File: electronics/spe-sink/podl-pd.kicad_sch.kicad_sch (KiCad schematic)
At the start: 18 parts, among them Q1 2N7002P, U1 ATL431LIB, U2 MCP65R41T, U3 AP7375-33

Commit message: PD function board schematic progress
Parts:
- added TEST3: CLIP_HOOK_GREY, Applidyne_Test:KEYSTONE_5118, symbol appli_test_points:CLIP_HOOK_GREY
- C1, C2, C3: footprint CAPC1608* -> Applidyne_Capacitor:CAPC1608X90N
- C4: footprint CAPC2012* -> Applidyne_Capacitor:CAPC2012X110N
- Q1: footprint SOT23 -> Applidyne_SOT:SOT95P240X110-3L16N
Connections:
- net PoDL+: now reaches C3.1, R4.1, R7.1, U3.1 (VIN)
- net PoDL+: now also TEST3.1 (PAD)
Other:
- note added: "Optional SCCP classification circuit would go here!"
- note removed: "Optional SCCP circuit would go here!"
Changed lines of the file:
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@@
   (junction (at 182.88 73.66) (diameter 0) (color 0 0 0 0)
   )
-  (wire (pts (xy 193.04 50.8) (xy 252.73 50.8))
+  (wire (pts (xy 193.04 50.8) (xy 222.25 50.8))
     (stroke (width 0) (type default))
   )
@@
     (effects (font (size 1.27 1.27)) (justify left bottom))
   )
-  (text "Optional SCCP circuit\nwould go here!" (at 223.52 64.77 0)
+  (text "Optional SCCP classification \ncircuit would go here!"
+    (at 228.6 58.42 0)
     (effects (font (size 1.27 1.27)) (justify left bottom))
   )
@@
     (at 198.12 130.81 0)
     (effects (font (size 1.27 1.27)) (justify left bottom))
+  )
+  (hierarchical_label "PoDL+" (shape input) (at 48.26 50.8 180) (fields_autoplaced)
+    (effects (font (size 1.27 1.27)) (justify right))
   )
   (symbol (lib_id "appli_capacitor:56n_X7R_1608M") (at 63.5 63.5 0) (unit 1)
@@
       (effects (font (size 0.889 0.889)) (justify right))
     )
-    (property "Footprint" "CAPC1608*" (at 66.548 65.532 90)
+    (property "Footprint" "Applidyne_Capacitor:CAPC1608X90N" (at 66.548 65.532 90)
       (effects (font (size 0.508 0.508)) hide)
     )
@@
     )
   )
+  (symbol (lib_id "appli_test_points:CLIP_HOOK_GREY") (at 222.25 50.8 270) (unit 1)
+    (in_bom yes) (on_board yes) (dnp no) (fields_autoplaced)
+    (property "Reference" "TEST3" (at 227.33 48.8949 90)
+      (effects (font (size 0.9906 0.9906)) (justify left))
+    )
+    (property "Value" "CLIP_HOOK_GREY" (at 222.25 52.07 0)
+      (effects (font (size 0.9906 0.9906)) (justify left top) hide)
+    )
+    (property "Footprint" "Applidyne_Test:KEYSTONE_5118" (at 220.98 52.07 0)
+      (effects (font (size 0.9906 0.9906)) (justify left top) hide)
+    )
+    (property "Datasheet" "http://www.farnell.com/datasheets/1703983.pdf" (at 217.17 52.07 0)
+      (effects (font (size 0.9906 0.9906)) (justify left bottom) hide)
+    )
+    (property "manf" "KEYSTONE" (at 219.71 52.07 0)
+      (effects (font (size 0.9906 0.9906)) (justify left top) hide)
+    )
+    (property "manf#" "5118" (at 215.9 52.07 0)
+      (effects (font (size 0.9906 0.9906)) (justify left bottom) hide)
+    )
+    (property "Supplier" "Element14" (at 214.63 52.07 0)
+      (effects (font (size 0.9906 0.9906)) (justify left bottom) hide)
+    )
+    (property "Supplier Part No" "2501304" (at 213.36 52.07 0)
+      (effects (font (size 0.9906 0.9906)) (justify left bottom) hide)
+    )
+    (property "Supplier URL" "http://au.element14.com/keystone/5118/test-point-pcb-grey-through-hole/dp/2501304" (at 212.09 52.07 0)
+      (effects (font (size 0.9906 0.9906)) (justify left bottom) hide)
+    )
+    (property "Supplier Price" "0.3" (at 210.82 52.07 0)
+      (effects (font (size 0.9906 0.9906)) (justify left bottom) hide)
+    )
+    (property "Suppier Price Break" "1" (at 209.55 52.07 0)
+      (effects (font (size 0.9906 0.9906)) (justify left bottom) hide)
+    )
+    (pin "1")
+    (instances
+      (project "spe-sink"
+        (path "/f0a501c7-1ad1-4c59-9255-3d6aa4545d8b/d425fecd-d9e0-4566-867f-2251b234bee9"
+          (reference "TEST3") (unit 1)
+        )
+      )
+    )
+  )
   (symbol (lib_id "appli_resistor:20K0_1608M") (at 182.88 74.93 0) (mirror y) (unit 1)
     (in_bom yes) (on_board yes) (dnp no) (fields_autoplaced)
@@
       (effects (font (size 0.889 0.889)) (justify left))
     )
-    (property "Footprint" "CAPC1608*" (at 150.241 81.28 90)
+    (property "Footprint" "Applidyne_Capacitor:CAPC1608X90N" (at 150.241 81.28 90)
       (effects (font (size 0.508 0.508)) hide)
     )
@@
       (effects (font (size 1.27 1.27)) (justify left))
     )
-    (property "Footprint" "SOT23" (at 195.58 99.06 0)
+    (property "Footprint" "Applidyne_SOT:SOT95P240X110-3L16N" (at 195.58 99.06 0)
       (effects (font (size 1.27 1.27) italic) (justify left) hide)
     )
@@
       (effects (font (size 0.889 0.889)) (justify left))
     )
-    (property "Footprint" "CAPC1608*" (at 114.681 106.68 90)
+    (property "Footprint" "Applidyne_Capacitor:CAPC1608X90N" (at 114.681 106.68 90)
       (effects (font (size 0.508 0.508)) hide)
     )
@@
       (effects (font (size 0.889 0.889)) (justify left))
     )
-    (property "Footprint" "CAPC2012*" (at 94.361 66.04 90)
-      (effects (font (size 0.508 0.508)) hide)
-    )
+    (property "Footprint" "Applidyne_Capacitor:CAPC2012X110N" (at 94.361 66.04 90)
+      (effects (font (size 0.508 0.508)) hide)
+    )

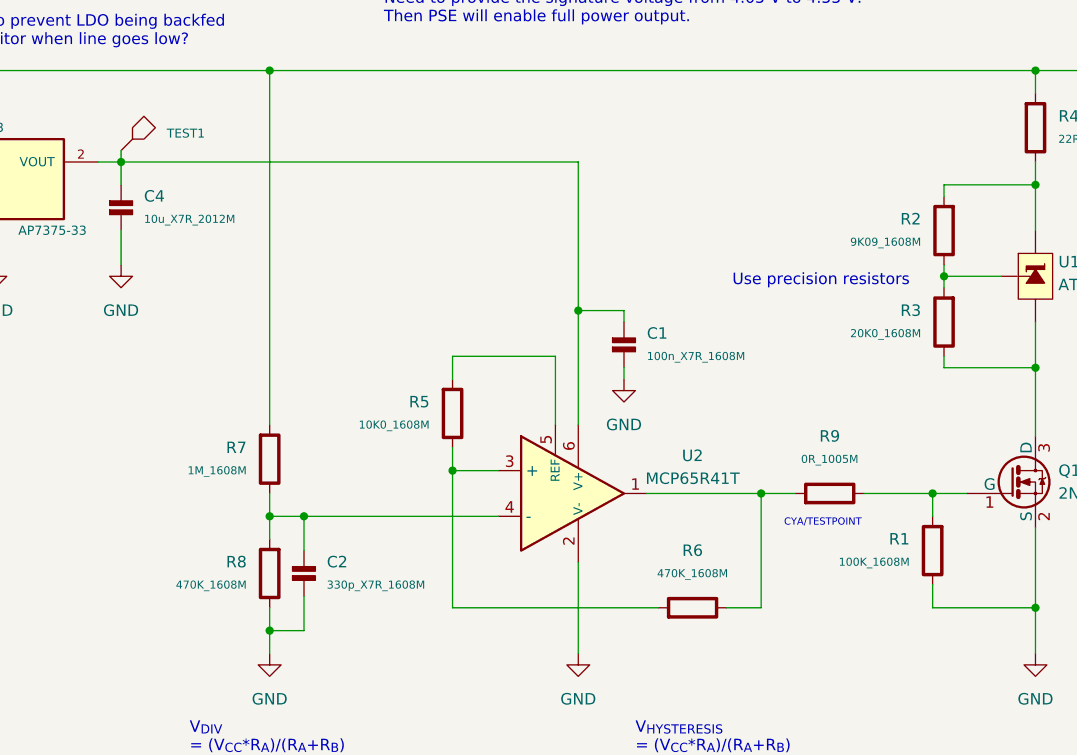
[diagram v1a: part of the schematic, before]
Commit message: PD function board bulk regulator, cleanup, part placement
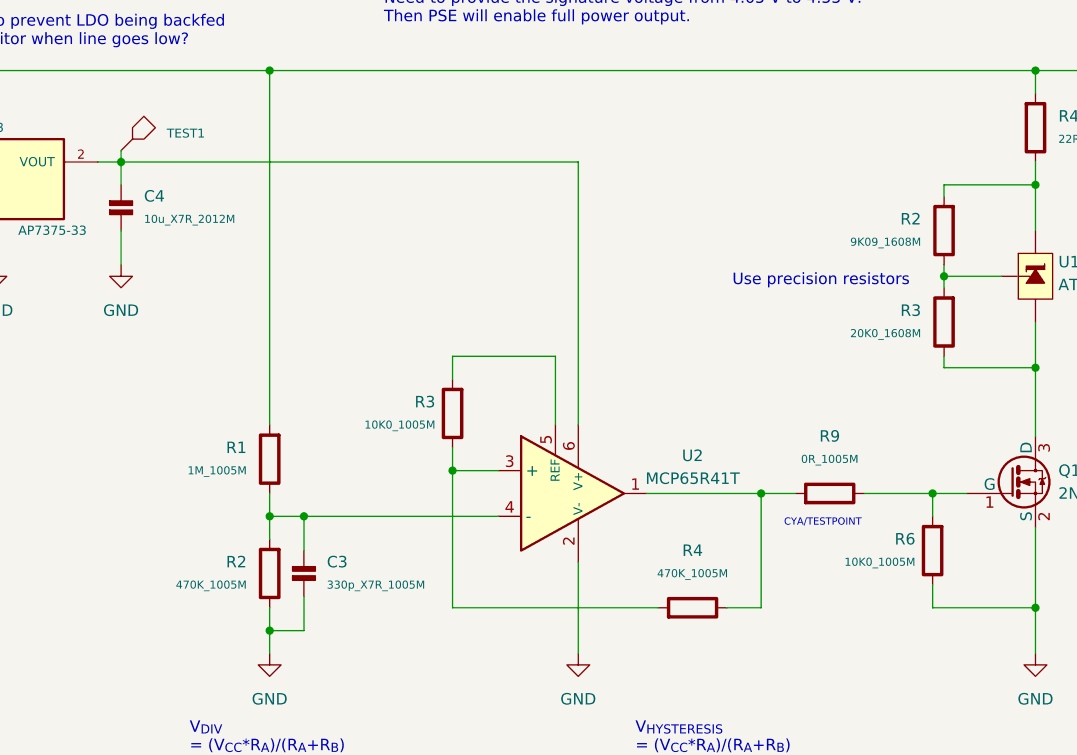
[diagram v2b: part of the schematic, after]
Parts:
- removed C1: 100n_X7R_1608M, Applidyne_Capacitor:CAPC1608X90N, symbol appli_capacitor:100n_X7R_1608M
- removed C2: 330p_X7R_1608M, Applidyne_Capacitor:CAPC1608X90N, symbol appli_capacitor:330p_X7R_1608M
- removed R1: 100K_1608M, Applidyne_Resistor:RESC1608X50N, symbol appli_resistor:100K_1608M
- removed R5: 10K0_1608M, Applidyne_Resistor:RESC1608X50N, symbol appli_resistor:10K0_1608M
- removed R6, R8: 470K_1608M, Applidyne_Resistor:RESC1608X50N, symbol appli_resistor:470K_1608M
- removed R7: 1M_1608M, Applidyne_Resistor:RESC1608X50N, symbol appli_resistor:1M_1608M
- added C3: 330p_X7R_1005M, Applidyne_Capacitor:CAPC1005X60N, symbol appli_capacitor:330p_X7R_1005M
- added R1: 1M_1005M, Applidyne_Resistor:RESC1005X40N, symbol appli_resistor:1M_1005M
- added R2, R4: 470K_1005M, Applidyne_Resistor:RESC1005X40N, symbol appli_resistor:470K_1005M
- added R3, R6: 10K0_1005M, Applidyne_Resistor:RESC1005X40N, symbol appli_resistor:10K0_1005M
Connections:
- net GND: now also C3.2, R2.2, R6.2
- net PoDL+: now also R1.1
- net at U2.4 (-): now also C3.1, R1.2, R2.1
- net at R9.1, U2.1: now also R4.2
- net at Q1.1 (G), R9.2: now also R6.1
- net at U2.3 (+): now also R3.2, R4.1
- net at U2.5 (REF): now also R3.1

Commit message: PD sink board routing, minor sch changes, etc
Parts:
- removed TEST1: CLIP_HOOK_ORANGE, Applidyne_Test:KEYSTONE_5003, symbol appli_test_points:CLIP_HOOK_ORANGE
- removed TEST3: CLIP_HOOK_GREY, Applidyne_Test:KEYSTONE_5118, symbol appli_test_points:CLIP_HOOK_GREY
- added TEST1: PROBE_PAD, Applidyne_Test:TP200, symbol appli_test_points:PROBE_PAD
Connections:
- net PoDL+: now also TEST1.1 (PAD)
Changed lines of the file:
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@@
-    (stroke (width 0) (type default))
-  )
-  (wire (pts (xy 91.44 59.69) (xy 91.44 60.96))
     (stroke (width 0) (type default))
   )
@@
     )
   )
-  (symbol (lib_id "appli_test_points:CLIP_HOOK_ORANGE") (at 91.44 59.69 270) (unit 1)
-    (in_bom yes) (on_board yes) (dnp no) (fields_autoplaced)
-    (property "Reference" "TEST1" (at 96.52 57.7849 90)
-      (effects (font (size 0.9906 0.9906)) (justify left))
-    )
-    (property "Value" "CLIP_HOOK_ORANGE" (at 91.44 60.96 0)
-      (effects (font (size 0.9906 0.9906)) (justify left top) hide)
-    )
-    (property "Footprint" "Applidyne_Test:KEYSTONE_5003" (at 90.17 60.96 0)
-      (effects (font (size 0.9906 0.9906)) (justify left top) hide)
-    )
-    (property "Datasheet" "http://www.farnell.com/datasheets/1703983.pdf" (at 86.36 60.96 0)
-      (effects (font (size 0.9906 0.9906)) (justify left bottom) hide)
-    )
-    (property "manf" "KEYSTONE" (at 88.9 60.96 0)
-      (effects (font (size 0.9906 0.9906)) (justify left top) hide)
-    )
-    (property "manf#" "5003" (at 85.09 60.96 0)
-      (effects (font (size 0.9906 0.9906)) (justify left bottom) hide)
-    )
-    (property "Supplier" "Element14" (at 83.82 60.96 0)
-      (effects (font (size 0.9906 0.9906)) (justify left bottom) hide)
-    )
-    (property "Supplier Part No" "2301280" (at 82.55 60.96 0)
-      (effects (font (size 0.9906 0.9906)) (justify left bottom) hide)
-    )
-    (property "Supplier URL" "http://au.element14.com/keystone/5003/test-point-pcb-through-hole/dp/2301280" (at 81.28 60.96 0)
-      (effects (font (size 0.9906 0.9906)) (justify left bottom) hide)
-    )
-    (property "Supplier Price" "0.261" (at 80.01 60.96 0)
-      (effects (font (size 0.9906 0.9906)) (justify left bottom) hide)
-    )
-    (property "Suppier Price Break" "100" (at 78.74 60.96 0)
-      (effects (font (size 0.9906 0.9906)) (justify left bottom) hide)
-    )
-    (pin "1")
-    (instances
-      (project "spe-sink"
-        (path "/f0a501c7-1ad1-4c59-9255-3d6aa4545d8b"
-          (reference "TEST1") (unit 1)
-        )
-        (path "/f0a501c7-1ad1-4c59-9255-3d6aa4545d8b/d425fecd-d9e0-4566-867f-2251b234bee9"
-          (reference "TEST1") (unit 1)
-        )
-      )
-    )
-  )
-  (symbol (lib_id "appli_test_points:CLIP_HOOK_GREY") (at 222.25 50.8 270) (unit 1)
-    (in_bom yes) (on_board yes) (dnp no) (fields_autoplaced)
-    (property "Reference" "TEST3" (at 227.33 48.8949 90)
-      (effects (font (size 0.9906 0.9906)) (justify left))
-    )
-    (property "Value" "CLIP_HOOK_GREY" (at 222.25 52.07 0)
-      (effects (font (size 0.9906 0.9906)) (justify left top) hide)
-    )
-    (property "Footprint" "Applidyne_Test:KEYSTONE_5118" (at 220.98 52.07 0)
-      (effects (font (size 0.9906 0.9906)) (justify left top) hide)
-    )
-    (property "Datasheet" "http://www.farnell.com/datasheets/1703983.pdf" (at 217.17 52.07 0)
-      (effects (font (size 0.9906 0.9906)) (justify left bottom) hide)
-    )
-    (property "manf" "KEYSTONE" (at 219.71 52.07 0)
-      (effects (font (size 0.9906 0.9906)) (justify left top) hide)
-    )
-    (property "manf#" "5118" (at 215.9 52.07 0)
-      (effects (font (size 0.9906 0.9906)) (justify left bottom) hide)
-    )
-    (property "Supplier" "Element14" (at 214.63 52.07 0)
-      (effects (font (size 0.9906 0.9906)) (justify left bottom) hide)
-    )
-    (property "Supplier Part No" "2501304" (at 213.36 52.07 0)
-      (effects (font (size 0.9906 0.9906)) (justify left bottom) hide)
-    )
-    (property "Supplier URL" "http://au.element14.com/keystone/5118/test-point-pcb-grey-through-hole/dp/2501304" (at 212.09 52.07 0)
-      (effects (font (size 0.9906 0.9906)) (justify left bottom) hide)
-    )
-    (property "Supplier Price" "0.3" (at 210.82 52.07 0)
-      (effects (font (size 0.9906 0.9906)) (justify left bottom) hide)
-    )
-    (property "Suppier Price Break" "1" (at 209.55 52.07 0)
-      (effects (font (size 0.9906 0.9906)) (justify left bottom) hide)
-    )
-    (pin "1")
-    (instances
-      (project "spe-sink"
-        (path "/f0a501c7-1ad1-4c59-9255-3d6aa4545d8b/d425fecd-d9e0-4566-867f-2251b234bee9"
-          (reference "TEST3") (unit 1)
-        )
-      )
-    )
-  )
   (symbol (lib_id "appli_resistor:20K0_1608M") (at 182.88 74.93 0) (mirror y) (unit 1)
     (in_bom yes) (on_board yes) (dnp no) (fields_autoplaced)
@@
         )
       )
+    )
+  )
+  (symbol (lib_id "appli_test_points:PROBE_PAD") (at 222.25 50.8 270) (unit 1)
+    (in_bom yes) (on_board yes) (dnp no) (fields_autoplaced)
+    (property "Reference" "TEST1" (at 219.71 50.8 0)
+      (effects (font (size 1.524 1.524)) hide)
+    )
+    (property "Value" "PROBE_PAD" (at 227.33 47.625 90)
+      (effects (font (size 1.524 1.524)) (justify left))
+    )
+    (property "Footprint" "Applidyne_Test:TP200" (at 227.33 48.895 90)
+      (effects (font (size 1.524 1.524)) (justify left) hide)
+    )
+    (property "Datasheet" "" (at 219.71 50.8 0)
+      (effects (font (size 1.524 1.524)))
+    )
+    (property "manf" "N/A" (at 208.28 50.8 0)
+      (effects (font (size 1.524 1.524)) hide)
+    )
+    (property "manf#" "N/A" (at 205.74 50.8 0)
+      (effects (font (size 1.524 1.524)) hide)
+    )
+    (property "Supplier" "N/A" (at 203.2 50.8 0)
+      (effects (font (size 1.524 1.524)) hide)
+    )
+    (property "Supplier URL" "#" (at 200.66 50.8 0)
+      (effects (font (size 1.524 1.524)) hide)
+    )
+    (property "Supplier Price" "0" (at 210.82 50.8 0)
+      (effects (font (size 1.524 1.524)) hide)
+    )
+    (property "Supplier Price Break" "0" (at 213.36 50.8 0)
+      (effects (font (size 1.524 1.524)) hide)
+    )
+    (property "Installed" "DNP" (at 227.33 50.165 90)
+      (effects (font (size 1.524 1.524)) (justify left))
+    )
+    (pin "1")
+    (instances
+      (project "spe-sink"
+        (path "/f0a501c7-1ad1-4c59-9255-3d6aa4545d8b/d425fecd-d9e0-4566-867f-2251b234bee9"
+          (reference "TEST1") (unit 1)
+        )
+      )

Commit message: PD sink PCB design 'finished', page cleanup, etc
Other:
- title: (none) -> SPE PD Detection Circuit
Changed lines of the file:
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@@
 (kicad_sch (version 20230121) (generator eeschema)
   (paper "A4")
+  (title_block
+    (title "SPE PD Detection Circuit")
+    (date "2023-08-16")
+    (rev "V1.0")
+    (comment 2 "as Fast-startup (no classification) hardware")
+    (comment 3 "Allows device to operate in class 10-12 (10-30V)")
+  )
   (junction (at 91.44 60.96) (diameter 0) (color 0 0 0 0)
   )

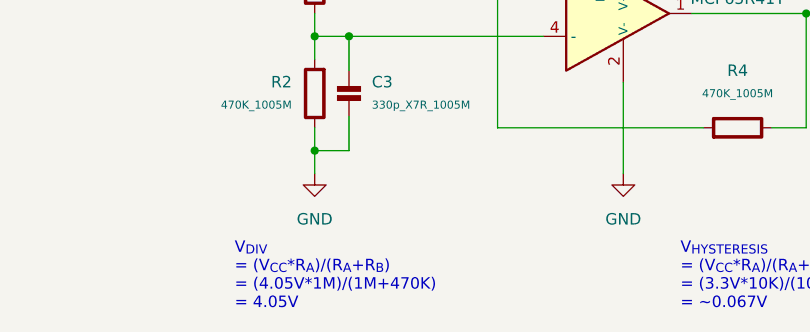
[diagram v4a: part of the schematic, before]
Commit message: Revised PSE input voltage limit resistor values
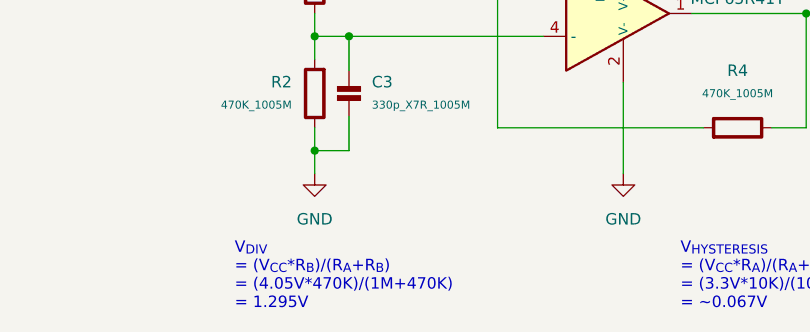
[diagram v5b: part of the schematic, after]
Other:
- note added: "V_{DIV} = (V_{CC}*R_{B})/(R_{A}+R_{B}) = (4.05V*470K)/(1M+470K) = 1.295V"
- note removed: "V_{DIV} = (V_{CC}*R_{A})/(R_{A}+R_{B}) = (4.05V*1M)/(1M+470K) = 4.05V"
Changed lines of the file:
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@@
     (effects (font (size 1.27 1.27)) (justify right bottom))
   )
-  (text "V_{DIV} \n= (V_{CC}*R_{A})/(R_{A}+R_{B})\n= (4.05V*1M)/(1M+470K)\n= 4.05V"
+  (text "V_{DIV} \n= (V_{CC}*R_{B})/(R_{A}+R_{B})\n= (4.05V*470K)/(1M+470K)\n= 1.295V"
     (at 99.06 130.81 0)
     (effects (font (size 1.27 1.27)) (justify left bottom))
